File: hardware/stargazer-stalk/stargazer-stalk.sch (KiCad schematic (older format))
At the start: 22 parts, among them U16 PCF8574

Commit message: Working before reworking to a 4 card system
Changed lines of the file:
@@
 CIPOx
 Text Label 2350 3850 0    50   ~ 0
-SCKn
+SCKx
 Text Label 2350 3950 0    50   ~ 0
 GOn
@@
 CIPOx
 Text Label 2350 4800 0    50   ~ 0
-SCKn
+SCKx
 Text Label 2350 4900 0    50   ~ 0
 GOn
@@
 CIPOx
 Text Label 2350 5750 0    50   ~ 0
-SCKn
+SCKx
 Text Label 2350 5850 0    50   ~ 0
 GOn
@@
 CIPOx
 Text Label 2350 6650 0    50   ~ 0
-SCKn
+SCKx
 Text Label 2350 6750 0    50   ~ 0
 GOn
@@
 CIPOx
 Text Label 5300 3850 0    50   ~ 0
-SCKn
+SCKx
 Text Label 5300 3950 0    50   ~ 0
 GOn
@@
 CIPOx
 Text Label 5300 4800 0    50   ~ 0
-SCKn
+SCKx
 Text Label 5300 4900 0    50   ~ 0
 GOn
@@
 CIPOx
 Text Label 5300 5750 0    50   ~ 0
-SCKn
+SCKx
 Text Label 5300 5850 0    50   ~ 0
 GOn
@@
 CIPOx
 Text Label 5300 6650 0    50   ~ 0
-SCKn
+SCKx
 Text Label 5300 6750 0    50   ~ 0
 GOn

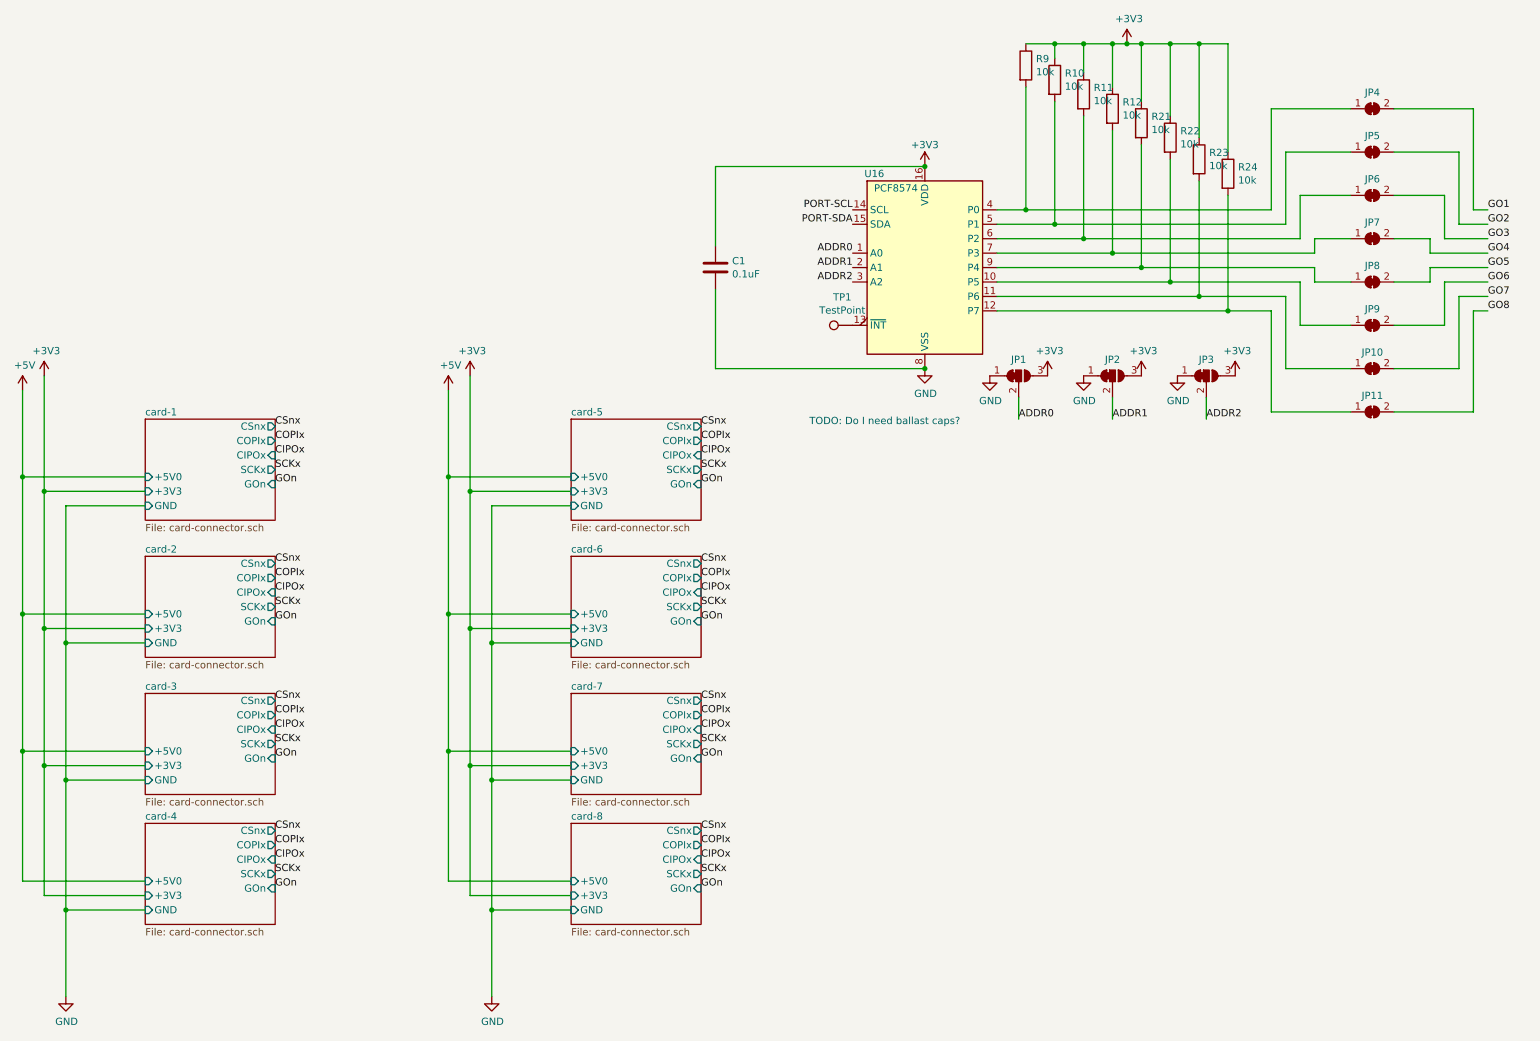
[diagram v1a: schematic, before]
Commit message: Finished routing, but it's probably too much for 2 layers
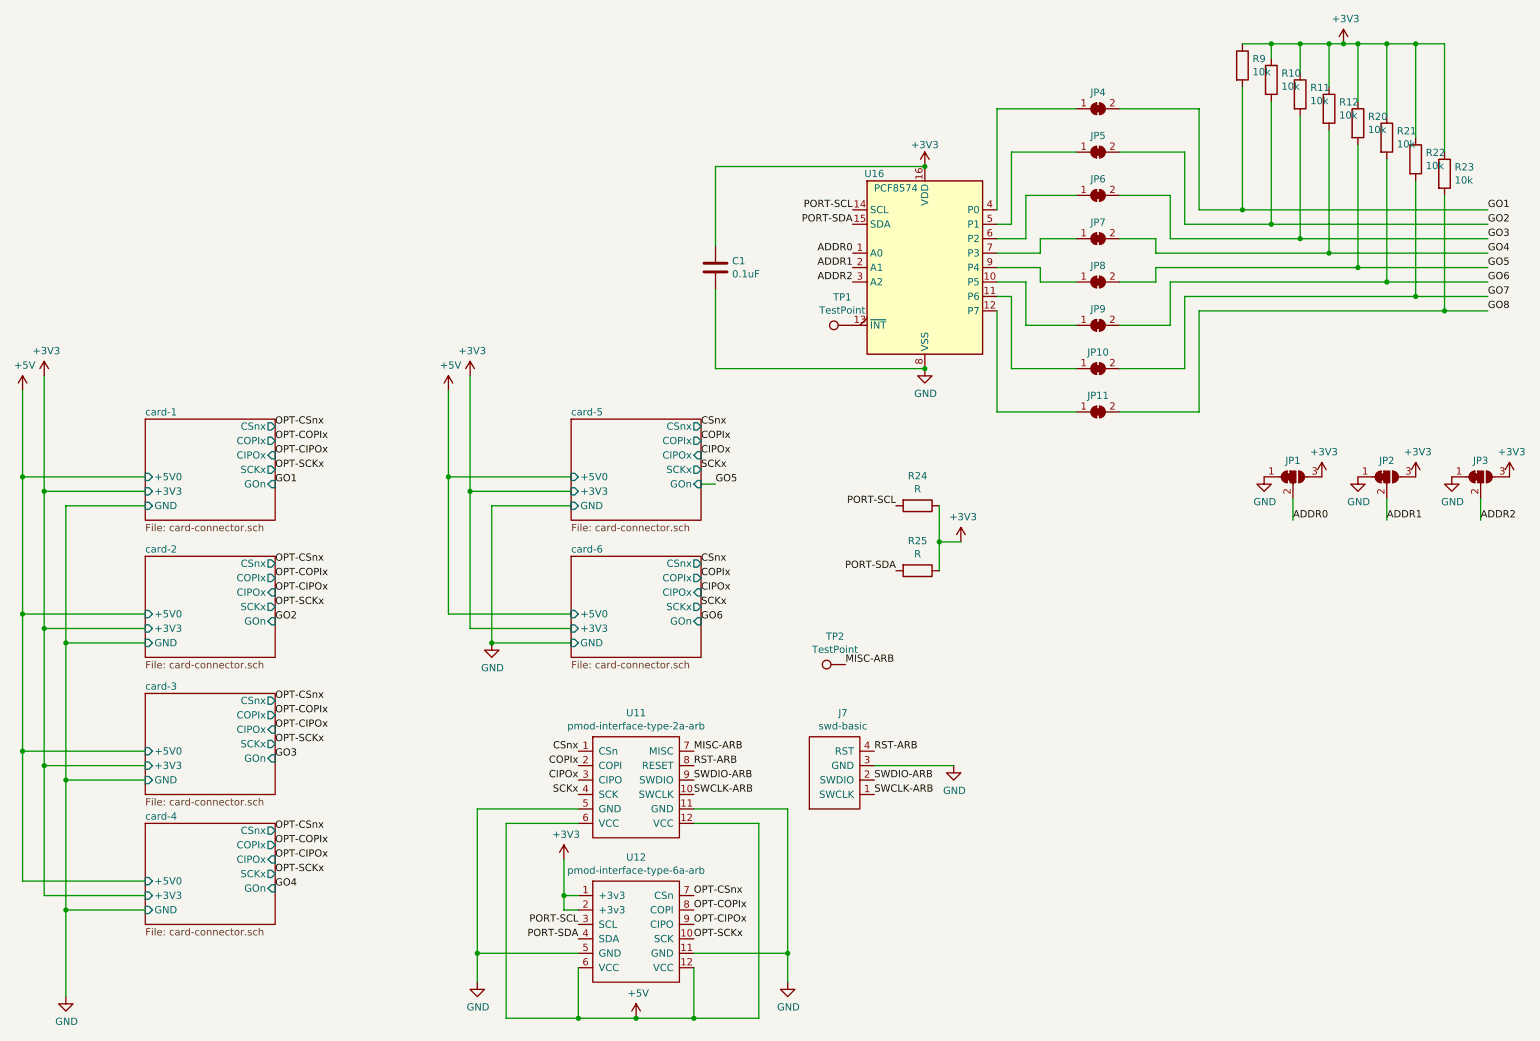
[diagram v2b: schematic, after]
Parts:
- added J7: swd-basic, Connector_PinHeader_2.54mm:PinHeader_1x04_P2.54mm_Vertical, symbol stargazer-stalk:swd-basic
- added R20: 10k, Resistor_SMD:R_0805_2012Metric, symbol Device:R
- added R25: R, Resistor_SMD:R_0805_2012Metric, symbol Device:R
- added TP2: TestPoint, Connector_PinHeader_2.54mm:PinHeader_1x01_P2.54mm_Vertical, symbol Connector:TestPoint
- added U11: pmod-interface-type-2a-arb, stargazer-stalk:pmod-double-vertical, symbol stargazer-stalk:pmod-interface-type-2a-arb
- added U12: pmod-interface-type-6a-arb, stargazer-stalk:pmod-double-vertical, symbol stargazer-stalk:pmod-interface-type-6a-arb
- R24: value 10k -> R
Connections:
- net +3V3: now also R20.1, R25.1, U12.1 (+3v3), U12.2 (+3v3)
- net +5V: now also U11.12 (VCC), U11.6 (VCC), U12.12 (VCC), U12.6 (VCC)
- net CIPOx: now also U11.3 (CIPO)
- net COPIx: now also U11.2 (COPI)
- net CSnx: now also U11.1 (CSn)
- net GND: now also J7.3 (GND), U11.11 (GND), U11.5 (GND), U12.11 (GND), U12.5 (GND)
- net GO1: now also R9.2
- net GO2: now also R10.2
- net GO3: now also R11.2
- net GO4: now also R12.2
- net GO5: now also R20.2
- net GO6: now also R21.2
- net GO7: now also R22.2
- net GO8: now also R23.2
- net PORT-SCL: now also R24.2, U12.3 (SCL)
- net PORT-SDA: now also R25.2, U12.4 (SDA)
- net SCKx: now also U11.4 (SCK)
- net at JP9.1 (A), U16.10 (P5): no longer R22.2
- net at JP10.1 (A), U16.11 (P6): no longer R23.2
- net at JP11.1 (A), U16.12 (P7): no longer R24.2
- net at JP4.1 (A), U16.4 (P0): no longer R9.2
- net at JP5.1 (A), U16.5 (P1): no longer R10.2
- net at JP6.1 (A), U16.6 (P2): no longer R11.2
- net at JP7.1 (A), U16.7 (P3): no longer R12.2
- net at JP8.1 (A), U16.9 (P4): no longer R21.2
- new net MISC-ARB: TP2.1, U11.7 (MISC)
- new net OPT-CIPOx: U12.9 (CIPO)
- new net OPT-COPIx: U12.8 (COPI)
- new net OPT-CSnx: U12.7 (CSn)
- new net OPT-SCKx: U12.10 (SCK)
- new net RST-ARB: J7.4 (RST), U11.8 (RESET)
- new net SWCLK-ARB: J7.1 (SWCLK), U11.10 (SWCLK)
- new net SWDIO-ARB: J7.2 (SWDIO), U11.9 (SWDIO)
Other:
- note removed: "TODO: Do I need ballast caps?\n"
- moved on the sheet: JP1, JP10, JP11, JP2, JP3, JP4, JP5, JP6, JP7, JP8, JP9
